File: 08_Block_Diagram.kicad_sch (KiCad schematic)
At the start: 1 part

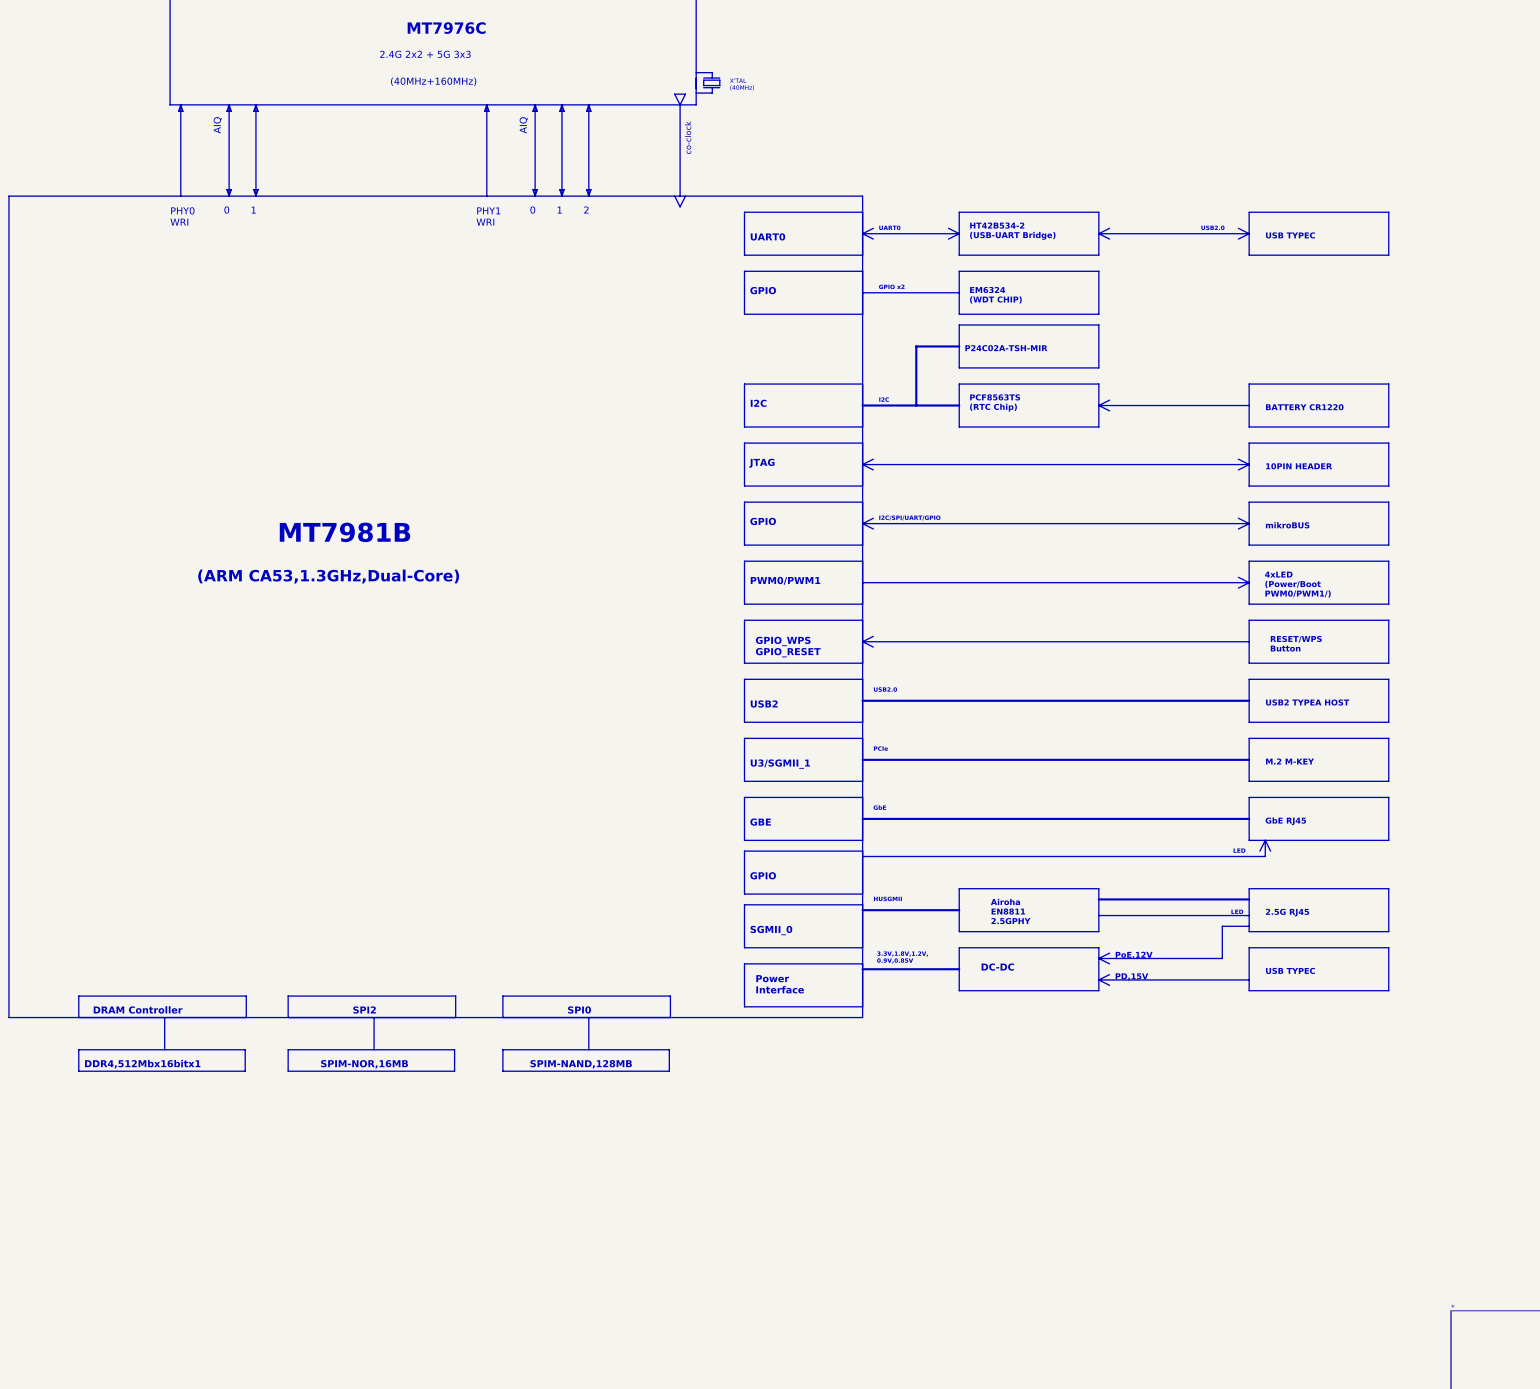
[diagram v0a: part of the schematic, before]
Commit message: Update to Kicad format 9
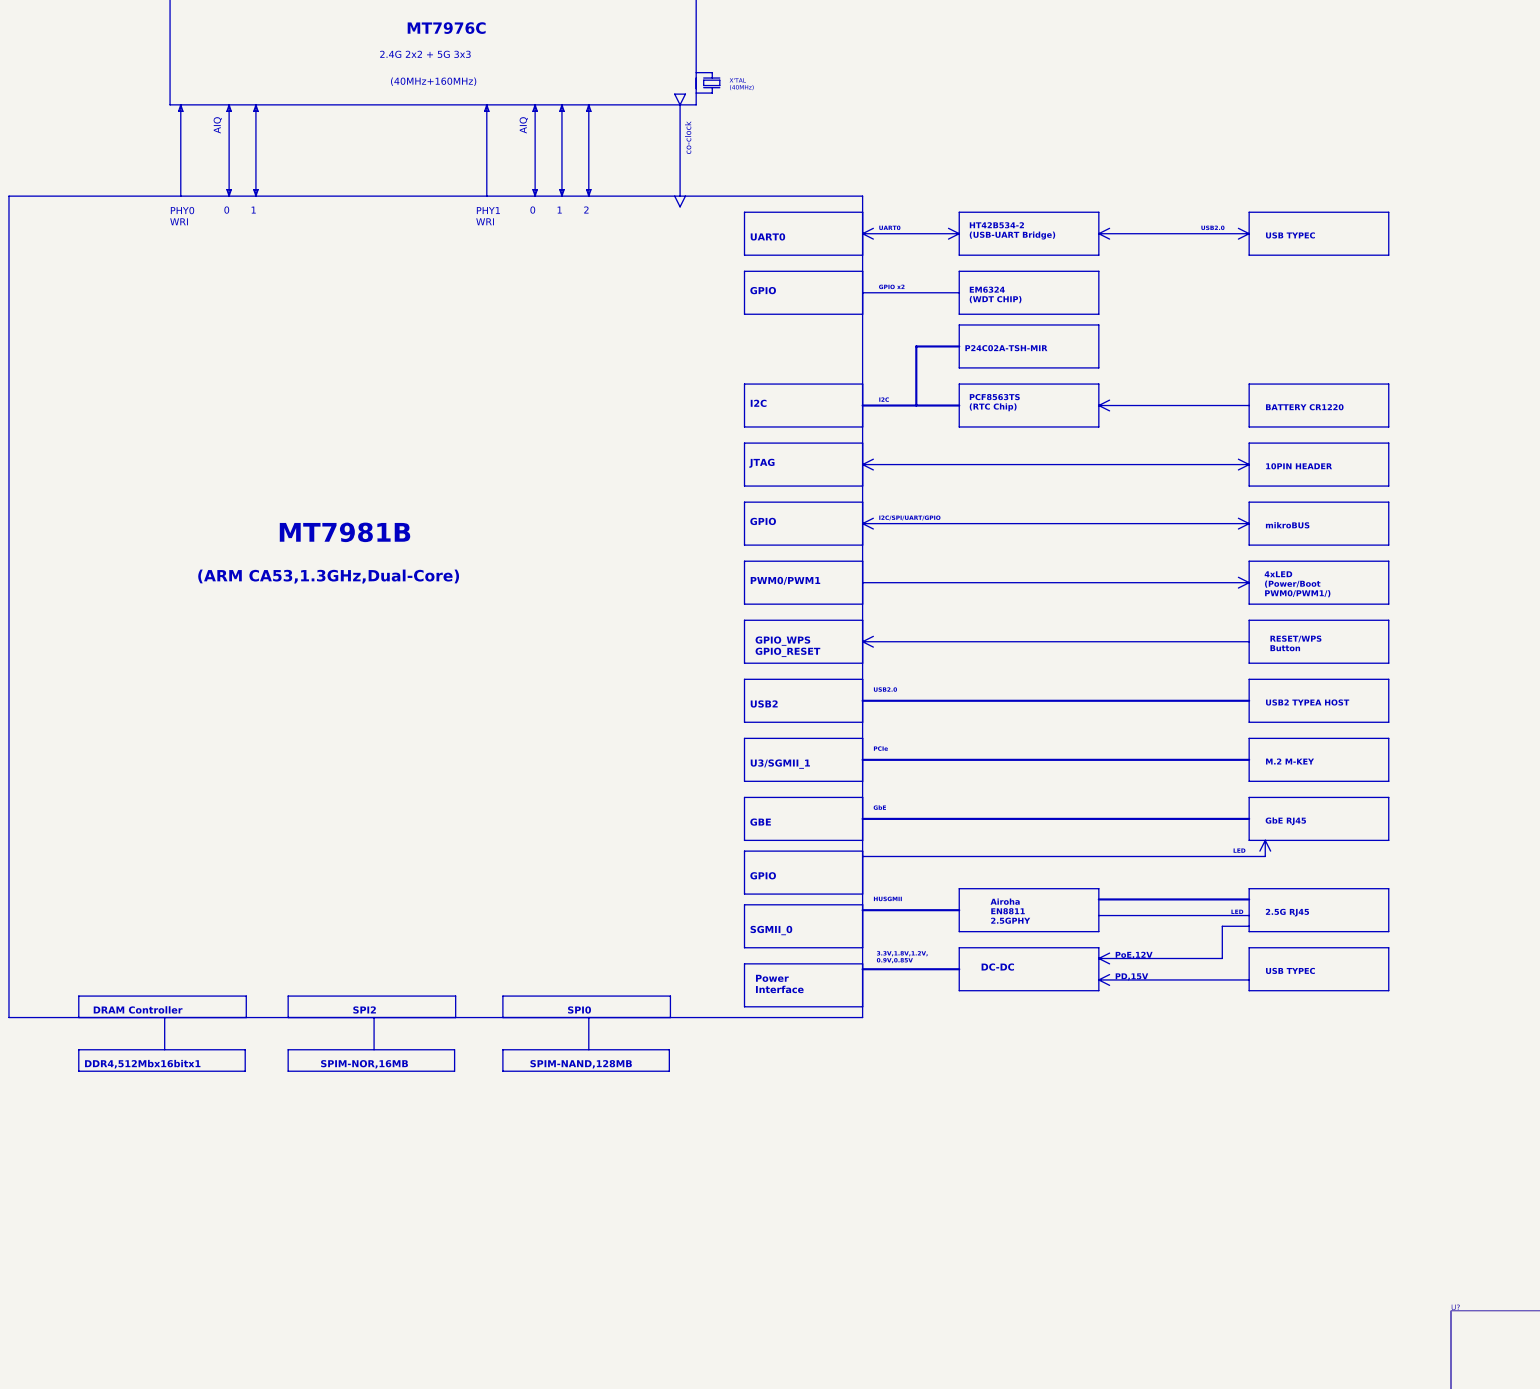
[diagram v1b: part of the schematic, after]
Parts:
- renumbered * to U?
